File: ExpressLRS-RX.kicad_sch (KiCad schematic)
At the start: 34 parts, among them J60 Conn_Coaxial, J61 Conn_01x01_Female, U60 ESP8285H16, U61 Crystal_ESP8285, U70 SX1280, U71 Crystal_SX1280

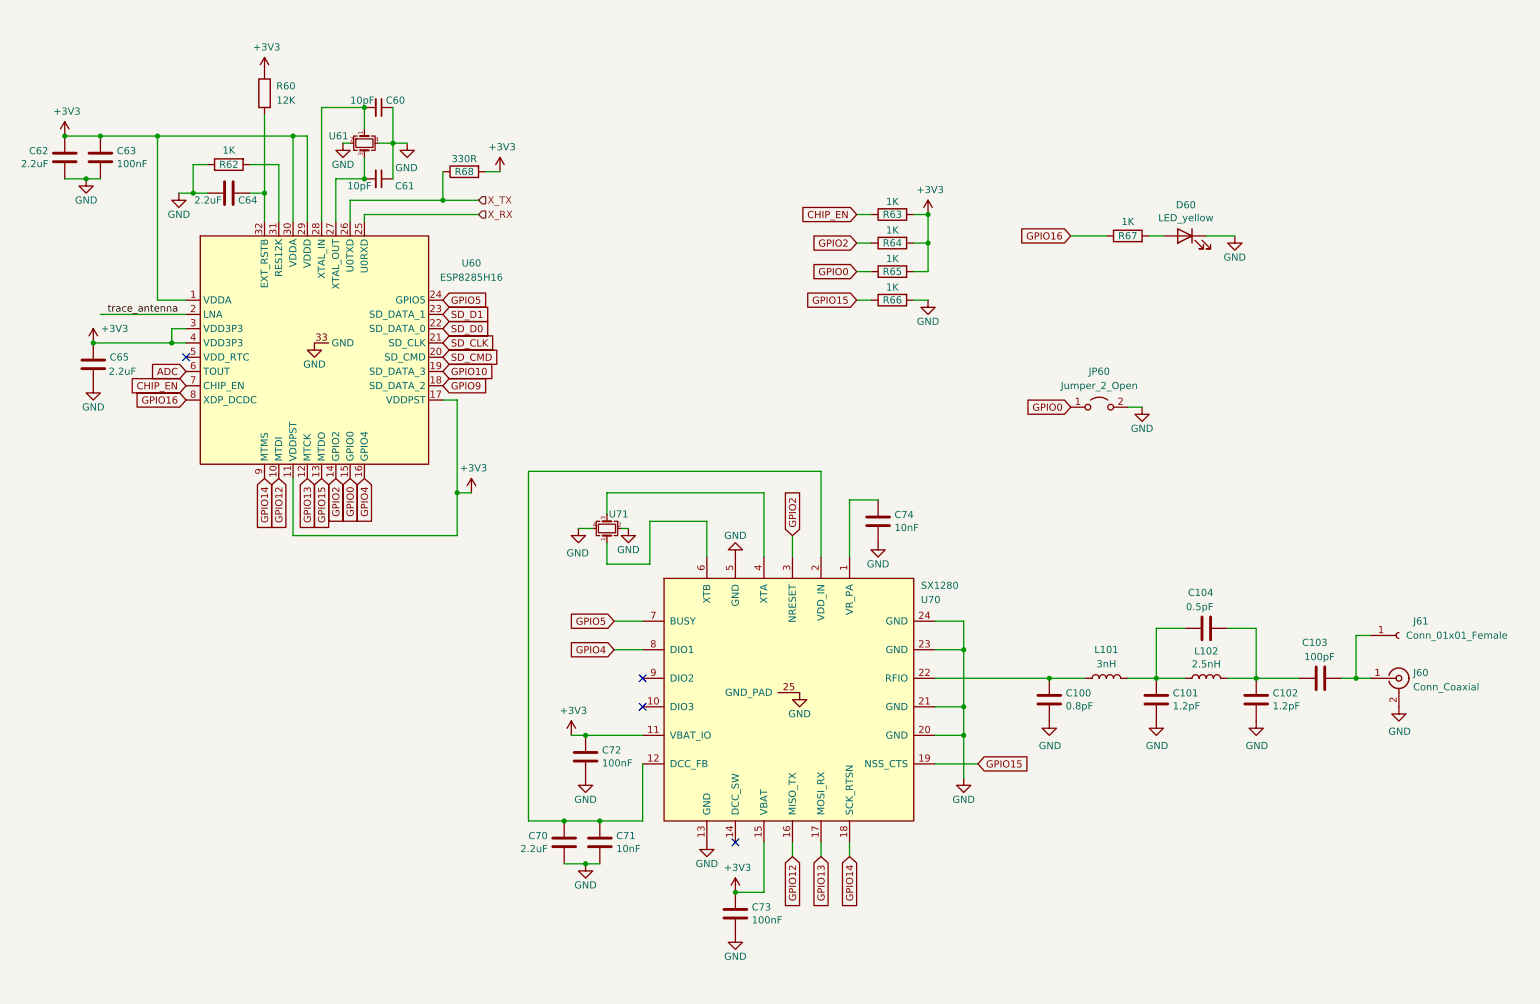
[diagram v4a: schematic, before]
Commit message: Cleaned up schematic
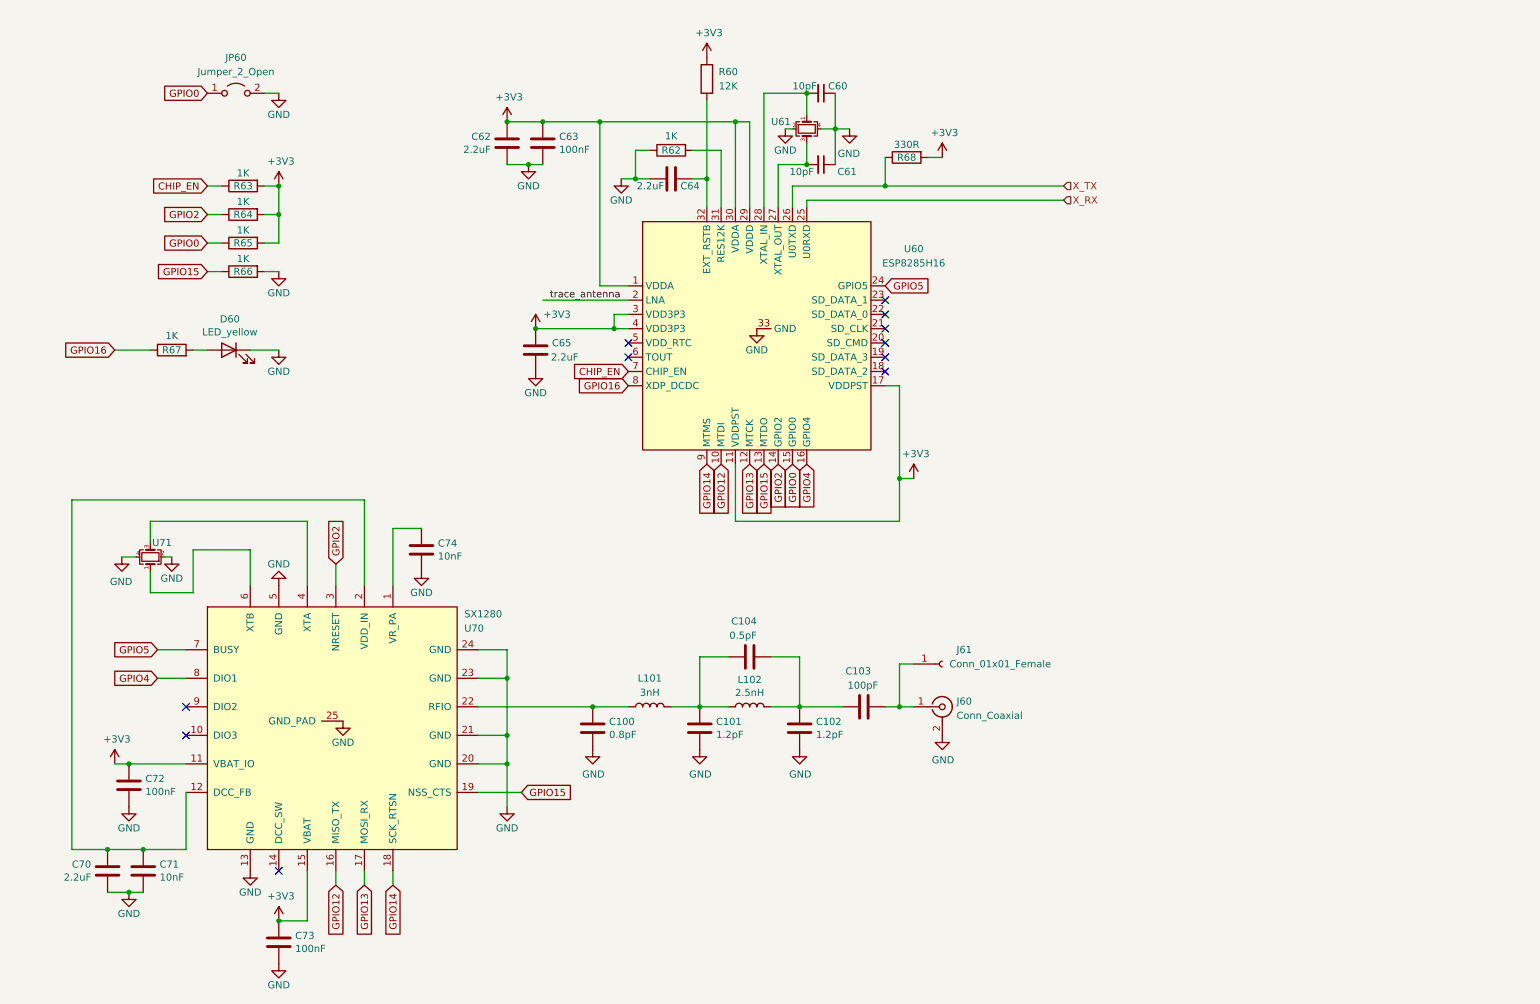
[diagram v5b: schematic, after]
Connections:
- net ADC: no longer names the net of U60.6 (TOUT)
- net GPIO10: no longer names the net of U60.19 (SD_DATA_3)
- net GPIO9: no longer names the net of U60.18 (SD_DATA_2)
- net SD_CLK: no longer names the net of U60.21 (SD_CLK)
- net SD_CMD: no longer names the net of U60.20 (SD_CMD)
- net SD_D0: no longer names the net of U60.22 (SD_DATA_0)
- net SD_D1: no longer names the net of U60.23 (SD_DATA_1)
- no-connect marks 4 -> 11
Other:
- title: spin-tgd-control -> ERLS RX
- moved on the sheet: C100, C101, C102, C103, C104, C60, C61, C62, C63, C64, C65, C70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
